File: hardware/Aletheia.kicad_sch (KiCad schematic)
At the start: 29 parts, among them J101 Conn_01x04, SW101 SW_DIP_x08, SW102 SW_DIP_x08, SW104 SW_DIP_x04, SW105 G19AP, U101 W65C02S6TPG-14, U102 AS6C1008-55PCN, U103 W65C22N6TPG-14, U104 74LS04, U105 74LS08, U106 74LS21, Y101 ECS-100AX-010

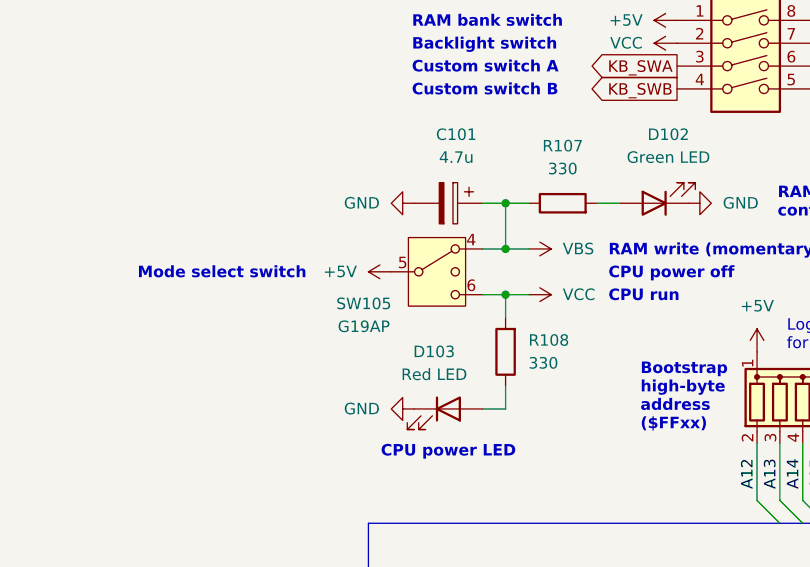
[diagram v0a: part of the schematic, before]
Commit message: Fix orientation of pins for mode switch in hardware
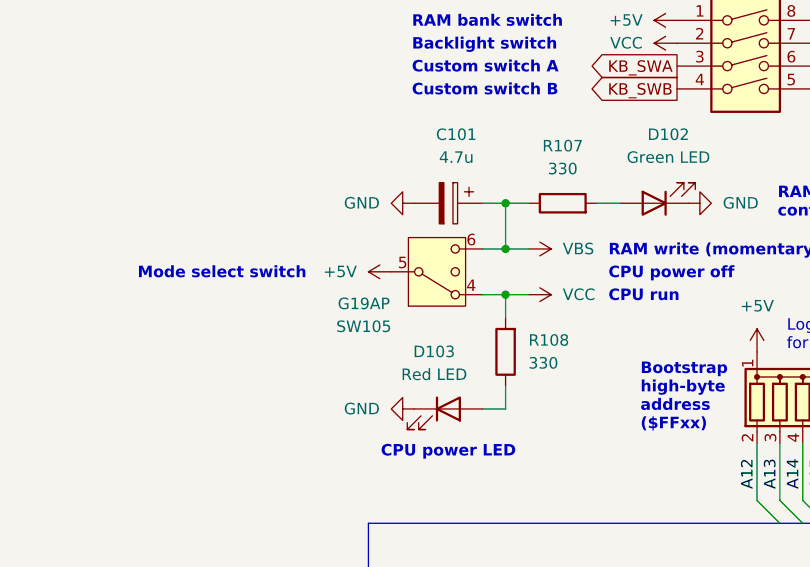
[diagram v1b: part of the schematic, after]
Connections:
- net VBS: now also SW105.6; no longer SW105.4
- net VCC: now also SW105.4; no longer SW105.6
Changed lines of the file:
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@@
 		(lib_id "Switch:SW_SPDT_MSM")
 		(at 53.34 59.69 0)
+		(mirror x)
 		(unit 1)
 		(exclude_from_sim no)
@@
 		(dnp no)
 		(property "Reference" "SW105"
+			(at 45.212 65.786 0)
+			(effects
+				(font
+					(size 1.27 1.27)
+				)
+			)
+		)
+		(property "Value" "G19AP"
 			(at 45.212 63.246 0)
 			(effects
@@
 			)
 		)
-		(property "Value" "G19AP"
-			(at 45.212 65.786 0)
-			(effects
-				(font
-					(size 1.27 1.27)
-				)
-			)
-		)
 		(property "Footprint" "Components:G19AP"
-			(at 39.37 48.26 0)
+			(at 39.37 71.12 0)
 			(effects
 				(font
@@
 		)
 		(property "Datasheet" "~"
-			(at 53.34 67.31 0)
+			(at 53.34 52.07 0)
 			(effects
 				(font
